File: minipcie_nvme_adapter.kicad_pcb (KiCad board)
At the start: 4 copper layers, 39.2 x 23.6 mm, 2 parts, among them J1 Bus_PCI_Express_Mini, J2 Bus_M.2_Socket_M

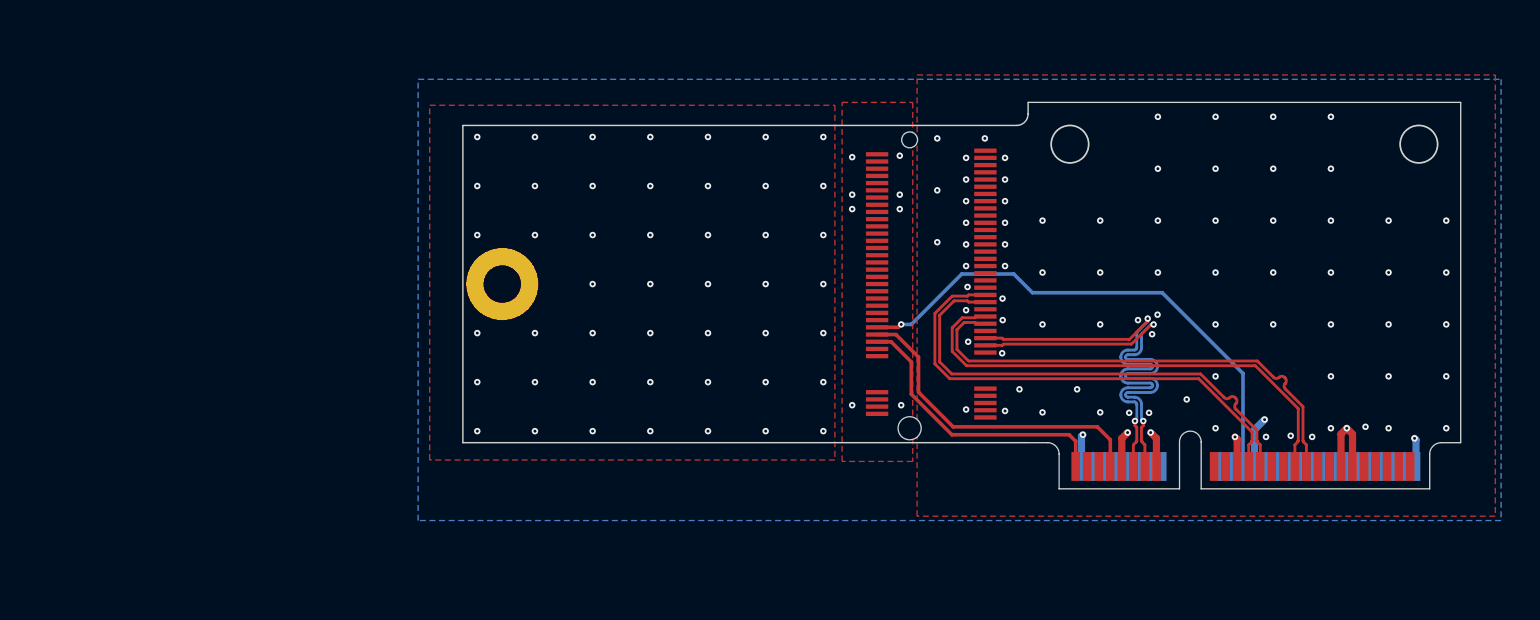
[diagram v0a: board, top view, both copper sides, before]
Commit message: Move m.2 connector right so that we can fit up to 2280 cards without exceeding 100mm width
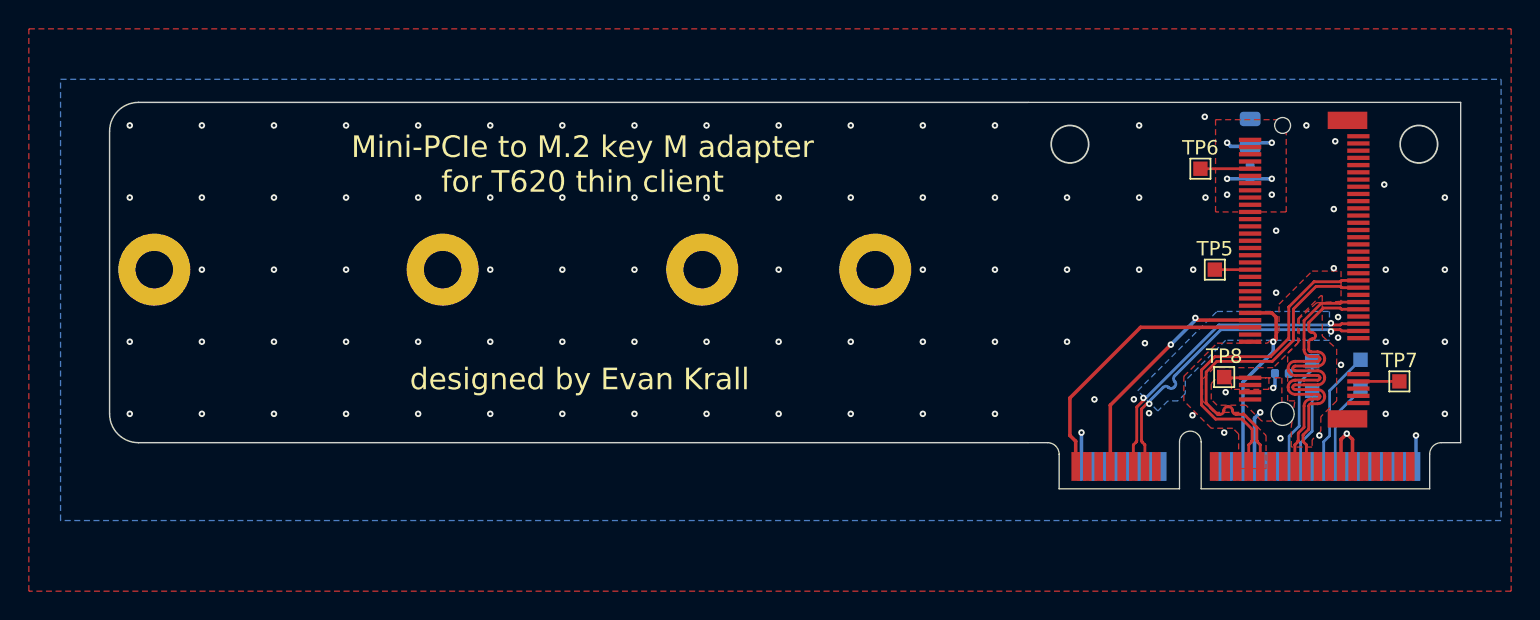
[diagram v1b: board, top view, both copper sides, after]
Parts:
- added C1: C, Capacitor_SMD:C_0805_2012Metric, B.Cu at (173.1, 69.6)
- added C2: C, Capacitor_SMD:C_0402_1005Metric, B.Cu at (173.1, 72.4)
- added C3: C, Capacitor_SMD:C_0402_1005Metric, B.Cu at (175.3, 86.3)
- added TP1: TestPoint, TestPoint:TestPoint_Pad_1.0x1.0mm, B.Cu at (177.4, 85.5)
- added TP2: TestPoint, TestPoint:TestPoint_Pad_1.0x1.0mm, B.Cu at (180.8, 85.3)
- added TP3: TestPoint, TestPoint:TestPoint_Pad_1.0x1.0mm, B.Cu at (177.4, 87.5)
- added TP4: TestPoint, TestPoint:TestPoint_Pad_1.0x1.0mm, B.Cu at (180.8, 87.5)
- added TP5: TestPoint, TestPoint:TestPoint_Pad_1.0x1.0mm, F.Cu at (170.7, 79.1)
- added TP6: TestPoint, TestPoint:TestPoint_Pad_1.0x1.0mm, F.Cu at (169.7, 72.1)
- added TP7: TestPoint, TestPoint:TestPoint_Pad_1.0x1.0mm, F.Cu at (183.4, 86.8)
- added TP8: TestPoint, TestPoint:TestPoint_Pad_1.0x1.0mm, F.Cu at (171.3, 86.5)
- moved J2 25.9 mm to (177.1, 79.1)
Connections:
- J1 pad 30: unconnected-(J1-Pad30) -> Net-(J1-Pad30)
- J1 pad 32: unconnected-(J1-Pad32) -> Net-(J1-Pad32)
- J1 pad 36: unconnected-(J1-Pad36) -> Net-(J1-Pad36)
- J1 pad 38: unconnected-(J1-Pad38) -> Net-(J1-Pad38)
- J2 pad 10: unconnected-(J2-Pad10) -> Net-(J2-Pad10)
- J2 pad 38: unconnected-(J2-Pad38) -> Net-(J2-Pad38)
- J2 pad 68: unconnected-(J2-Pad68) -> Net-(J2-Pad68)
- J2 pad 69: unconnected-(J2-Pad69) -> Net-(J2-Pad69)
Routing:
- net /~{PERST}: track 36.2 -> 13.2 mm
- net /PET_0+: track 34.0 -> 23.9 mm
- net /PET_0-: track 34.0 -> 23.9 mm
- net /PER_0-: track 34.0 -> 24.0 mm
- net /PER_0+: track 34.0 -> 24.1 mm
- net /REFCLK-: track 32.0 -> 22.2 mm
- net /REFCLK+: track 32.0 -> 22.2 mm
- net Net-(J1-Pad36): track 0.00 -> 8.46 mm
- net Net-(J1-Pad30): track 0.00 -> 7.96 mm
- net /3.3V: track 13.4 -> 20.8 mm
- net GND: track 7.14 -> 0.00 mm, vias 127 -> 95
- net Net-(J1-Pad38): track 0.00 -> 6.02 mm
- net /~{CLKREQ}: track 22.5 -> 16.6 mm, vias 0 -> 2
- net Net-(J1-Pad32): track 0.00 -> 5.58 mm
- net Net-(J2-Pad10): track 0.00 -> 3.44 mm
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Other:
- board size 39.2 x 23.6 mm -> 63.7 x 23.6 mm
- board text added: "JLCJLCJLCJLC"
- board text added: "Mini-PCIe to M.2 key M adapter for T620 thin client"
- board text added: "designed by Evan Krall"
